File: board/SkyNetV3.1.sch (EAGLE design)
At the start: 48 parts, among them IC2 RF4463PRO, IC3 LPC1769, IC4 BCX17, Q1 32.768KHz, Q2 12MHz, U1 MCP16301T-I/CHY, X2 CONN-SMATHD

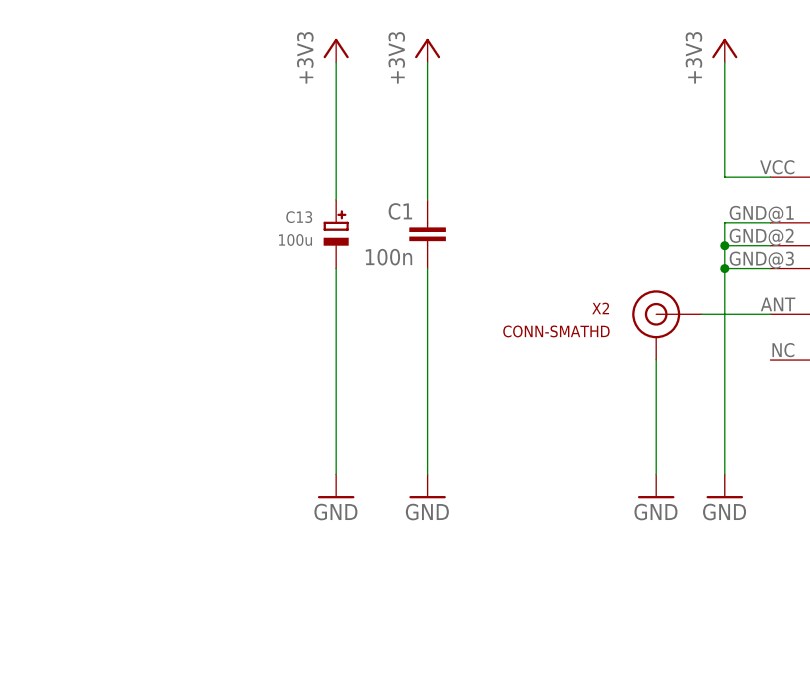
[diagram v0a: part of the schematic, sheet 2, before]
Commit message: improved placement
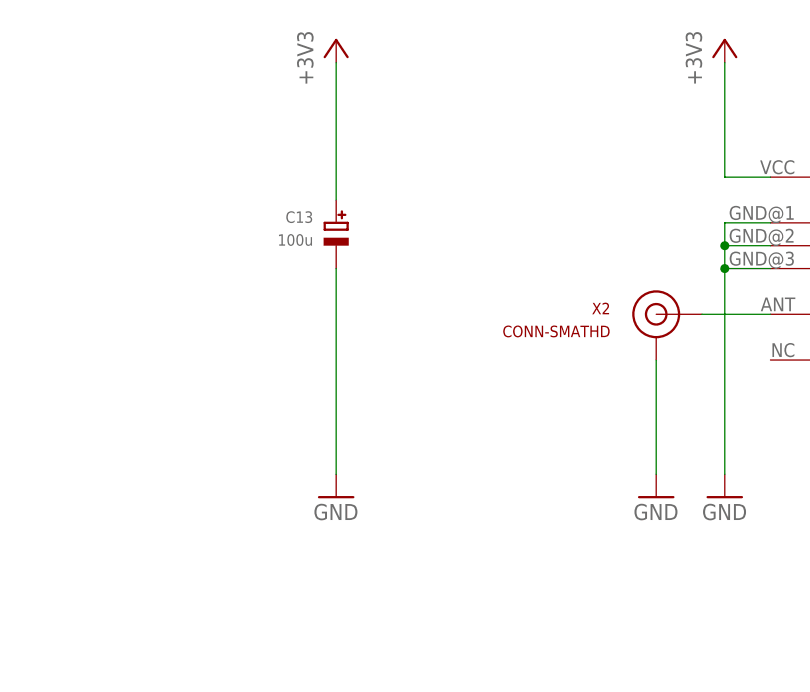
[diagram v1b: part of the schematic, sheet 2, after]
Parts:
- removed C1: 100n, rcl:C-EUC1206K
- C7: value (none) -> 100n
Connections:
- net +3V3: no longer C1.1
- net GND: no longer C1.2
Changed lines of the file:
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@@
 <part name="R5" library="rcl" deviceset="R-EU_" device="R0603" value="10K"/>
 <part name="IC2" library="RF4436PRO" deviceset="RF4463PRO" device=""/>
-<part name="GND10" library="supply1" deviceset="GND" device=""/>
 <part name="+3V1" library="supply1" deviceset="+3V3" device=""/>
 <part name="+3V5" library="supply1" deviceset="+3V3" device=""/>
@@
 <part name="+3V15" library="supply1" deviceset="+3V3" device=""/>
 <part name="R1" library="rcl" deviceset="R-EU_" device="R0603" value="10k"/>
-<part name="C1" library="rcl" deviceset="C-EU" device="C1206K" value="100n"/>
 <part name="P+10" library="supply1" deviceset="+5V" device=""/>
 <part name="GND23" library="supply1" deviceset="GND" device=""/>
@@
 <part name="C6" library="rcl" deviceset="C-EU" device="C0805" value="10u"/>
 <part name="+3V6" library="supply1" deviceset="+3V3" device=""/>
-<part name="+3V7" library="supply1" deviceset="+3V3" device=""/>
 <part name="+3V11" library="supply1" deviceset="+3V3" device=""/>
 <part name="JP3" library="microbuilder" deviceset="HEADER-2X5" device="1.27MM" value="JTAG"/>
@@
 <part name="U1" library="skynet_other" deviceset="MCP16301T-I/CHY" device=""/>
 <part name="GND3" library="supply1" deviceset="GND" device=""/>
-<part name="C7" library="rcl" deviceset="C-EU" device="C0603"/>
+<part name="C7" library="rcl" deviceset="C-EU" device="C0603" value="100n"/>
 <part name="D1" library="microbuilder" deviceset="DIODE" device="SOD-323" value="1N4148 WS"/>
 <part name="B140F" library="diode" deviceset="DIODE-" device="DO214AC"/>
@@
 <instance part="FRAME4" gate="G$1" x="0" y="0"/>
 <instance part="IC2" gate="G$1" x="152.4" y="106.68"/>
-<instance part="GND10" gate="1" x="99.06" y="81.28"/>
-<instance part="C1" gate="G$1" x="99.06" y="111.76" rot="MR0"/>
 <instance part="C13" gate="G$1" x="88.9" y="109.22" rot="MR0"/>
 <instance part="GND19" gate="1" x="88.9" y="81.28"/>
@@
 <instance part="GND32" gate="1" x="124.46" y="81.28"/>
 <instance part="+3V6" gate="G$1" x="88.9" y="132.08"/>
-<instance part="+3V7" gate="G$1" x="99.06" y="132.08"/>
 <instance part="+3V11" gate="G$1" x="132.08" y="132.08"/>
 </instances>
@@
 <nets>
 <net name="GND" class="0">
-<segment>
-<pinref part="C1" gate="G$1" pin="2"/>
-<pinref part="GND10" gate="1" pin="GND"/>
-<wire x1="99.06" y1="83.82" x2="99.06" y2="106.68" width="0.1524" layer="91"/>
-</segment>
 <segment>
 <pinref part="GND19" gate="1" pin="GND"/>
@@
 </segment>
 <segment>
-<pinref part="C1" gate="G$1" pin="1"/>
-<pinref part="+3V7" gate="G$1" pin="+3V3"/>
-<wire x1="99.06" y1="129.54" x2="99.06" y2="114.3" width="0.1524" layer="91"/>
-</segment>
-<segment>

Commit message: almost done
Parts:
- removed C9: 10u, rcl:C-EUC0805
- removed SJ1: RESET, jumper:SJ
- removed USB1: MOLEX-47346-0001, usb_con-update:MOLEX-47346-0001
- added JP1: (no value), jumper:JP1E
- added TP4, TP5: PTR1B1,27, testpad:PTR1B1,27
- added TP6: PTR1B2,54, testpad:PTR1B2,54
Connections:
- net +3V3: now also TP6.TP; no longer C9.1
- net +5V: now also JP1.2; no longer USB1.1
- net GND: now also JP1.1; no longer C9.2, SJ1.1, USB1.5, USB1.GND1, USB1.GND2, USB1.GND3, USB1.GND4
- net RESET: no longer SJ1.2
- net USB-CABLE-D+: now also TP5.TP; no longer USB1.3
- net USB-CABLE-D-: now also TP4.TP; no longer USB1.2
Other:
- moved on the sheet: R2

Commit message: mitten drin
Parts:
- added TP10, TP11, TP12, TP13, TP7, TP8, TP9: PTR1B1,27, testpad:PTR1B1,27
- TP3: value PTR1B1,27 -> PTR1B2,54; device testpad:PTR1B1,27 -> testpad:PTR1B2,54
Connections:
- new net N$10: IC3.P2[13]/EINT3/I2STX_SDA, TP13.TP
- new net N$3: IC3.P2[0]/PWM1[1]/TXD1, TP8.TP
- new net N$5: IC3.P0[9]/I2STX_SDA/MOSI1/MAT2[3], TP9.TP
- new net N$6: IC3.P0[8]/I2STX_WS/MISO1/MAT2[2], TP10.TP
- new net N$7: IC3.P2[1]/PWM1[2]/RXD1, TP7.TP
- new net N$8: IC3.P0[11]/RXD2/SCL2/MAT3[1], TP12.TP
- new net N$9: IC3.P0[10]/TXD2/SDA2/MAT3[0], TP11.TP
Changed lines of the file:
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@@
 <part name="+3V12" library="supply1" deviceset="+3V3" device=""/>
 <part name="GND14" library="supply1" deviceset="GND" device=""/>
-<part name="TP3" library="testpad" deviceset="PTR1" device="B1,27"/>
 <part name="GND1" library="supply1" deviceset="GND" device=""/>
 <part name="U1" library="skynet_other" deviceset="MCP16301T-I/CHY" device=""/>
@@
 <part name="TP6" library="testpad" deviceset="PTR1" device="B2,54"/>
 <part name="+3V7" library="supply1" deviceset="+3V3" device=""/>
+<part name="TP7" library="testpad" deviceset="PTR1" device="B1,27"/>
+<part name="TP8" library="testpad" deviceset="PTR1" device="B1,27"/>
+<part name="TP9" library="testpad" deviceset="PTR1" device="B1,27"/>
+<part name="TP10" library="testpad" deviceset="PTR1" device="B1,27"/>
+<part name="TP11" library="testpad" deviceset="PTR1" device="B1,27"/>
+<part name="TP12" library="testpad" deviceset="PTR1" device="B1,27"/>
+<part name="TP3" library="testpad" deviceset="PTR1" device="B2,54"/>
+<part name="TP13" library="testpad" deviceset="PTR1" device="B1,27"/>
 </parts>
 <sheets>
@@
 <instance part="R1" gate="G$1" x="60.96" y="40.64" rot="R90"/>
 <instance part="SJ2" gate="1" x="215.9" y="45.72" rot="R90"/>
+<instance part="TP7" gate="G$1" x="167.64" y="99.06" rot="R90"/>
+<instance part="TP8" gate="G$1" x="167.64" y="101.6" rot="R90"/>
+<instance part="TP9" gate="G$1" x="45.72" y="142.24" rot="R270"/>
+<instance part="TP10" gate="G$1" x="45.72" y="144.78" rot="R270"/>
+<instance part="TP11" gate="G$1" x="45.72" y="139.7" rot="R270"/>
+<instance part="TP12" gate="G$1" x="45.72" y="137.16" rot="R270"/>
+<instance part="TP13" gate="G$1" x="167.64" y="68.58" rot="R90"/>
 </instances>
 <busses>
@@
 <wire x1="198.12" y1="99.06" x2="223.52" y2="99.06" width="0.1524" layer="91"/>
 <label x="223.52" y="99.06" size="1.27" layer="95" xref="yes"/>
+</segment>
+</net>
+<net name="N$3" class="0">
+<segment>
+<pinref part="IC3" gate="G$1" pin="P2[0]/PWM1[1]/TXD1"/>
+<pinref part="TP8" gate="G$1" pin="TP"/>
+<wire x1="165.1" y1="101.6" x2="160.02" y2="101.6" width="0.1524" layer="91"/>
+</segment>
+</net>
+<net name="N$5" class="0">
+<segment>
+<pinref part="IC3" gate="G$1" pin="P0[9]/I2STX_SDA/MOSI1/MAT2[3]"/>
+<pinref part="TP9" gate="G$1" pin="TP"/>
+<wire x1="48.26" y1="142.24" x2="71.12" y2="142.24" width="0.1524" layer="91"/>
+</segment>
+</net>
+<net name="N$6" class="0">
+<segment>
+<pinref part="IC3" gate="G$1" pin="P0[8]/I2STX_WS/MISO1/MAT2[2]"/>
+<pinref part="TP10" gate="G$1" pin="TP"/>
+<wire x1="48.26" y1="144.78" x2="71.12" y2="144.78" width="0.1524" layer="91"/>
+</segment>
+</net>
+<net name="N$7" class="0">
+<segment>
+<pinref part="IC3" gate="G$1" pin="P2[1]/PWM1[2]/RXD1"/>
+<pinref part="TP7" gate="G$1" pin="TP"/>
+<wire x1="165.1" y1="99.06" x2="160.02" y2="99.06" width="0.1524" layer="91"/>
+</segment>
+</net>
+<net name="N$8" class="0">
+<segment>
+<pinref part="IC3" gate="G$1" pin="P0[11]/RXD2/SCL2/MAT3[1]"/>
+<pinref part="TP12" gate="G$1" pin="TP"/>
+<wire x1="48.26" y1="137.16" x2="71.12" y2="137.16" width="0.1524" layer="91"/>
+</segment>
+</net>
+<net name="N$9" class="0">
+<segment>
+<pinref part="IC3" gate="G$1" pin="P0[10]/TXD2/SDA2/MAT3[0]"/>
+<pinref part="TP11" gate="G$1" pin="TP"/>
+<wire x1="48.26" y1="139.7" x2="71.12" y2="139.7" width="0.1524" layer="91"/>
+</segment>
+</net>
+<net name="N$10" class="0">
+<segment>
+<pinref part="IC3" gate="G$1" pin="P2[13]/EINT3/I2STX_SDA"/>
+<pinref part="TP13" gate="G$1" pin="TP"/>
+<wire x1="165.1" y1="68.58" x2="160.02" y2="68.58" width="0.1524" layer="91"/>
 </segment>
 </net>
@@
 <instance part="+3V12" gate="G$1" x="45.72" y="71.12"/>
 <instance part="GND14" gate="1" x="45.72" y="33.02"/>
-<instance part="TP3" gate="G$1" x="195.58" y="48.26" rot="R270"/>
 <instance part="GND1" gate="1" x="203.2" y="40.64"/>
 <instance part="TP4" gate="G$1" x="35.56" y="139.7" rot="R270"/>
@@
 <instance part="TP6" gate="G$1" x="200.66" y="106.68" rot="R90"/>
 <instance part="+3V7" gate="G$1" x="195.58" y="106.68" rot="MR270"/>
+<instance part="TP3" gate="G$1" x="195.58" y="48.26" rot="R270"/>
 </instances>
 <busses>
@@
 </segment>
 <segment>
-<pinref part="TP3" gate="G$1" pin="TP"/>
 <pinref part="GND1" gate="1" pin="GND"/>
 <wire x1="198.12" y1="48.26" x2="203.2" y2="48.26" width="0.1524" layer="91"/>
 <wire x1="203.2" y1="48.26" x2="203.2" y2="43.18" width="0.1524" layer="91"/>
-</segment>
-</net>
+<pinref part="TP3" gate="G$1" pin="TP"/>
+</segment>
+</net>

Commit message: done
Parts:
- removed C18: 100n, rcl:C-EUC0603
- removed LED2: RGBLED5050, adafruit:RGBLED5050
- removed R18, R19: 68, rcl:R-EU_R0603
- added LED1: (no value), led:LEDCHIP-LED0805
- R17: value 100 -> 360
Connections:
- removed net LED-B: IC3.P1[18]/USB_UP_LED/PWM1[1]/CAP1[0], LED2.BLUE_C
- removed net LED-B-R: LED2.BLUE_A, R19.1
- removed net LED-G: IC3.P1[21]/MCABORT/PWM1[3]/SSEL0, LED2.GREEN_C
- removed net LED-G-R: LED2.GREEN_A, R18.1
- removed net LED-R: IC3.P1[20]/MCI0/PWM1[2]/SCK0, LED2.RED_C
- new net LED: IC3.P1[21]/MCABORT/PWM1[3]/SSEL0, LED1.C
- net +3V3: no longer C18.1, R18.2, R19.2
- net GND: no longer C18.2
- net LED-R-R: now also LED1.A; no longer LED2.RED_A
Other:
- note removed: "TODO: I2C ADC??"
- moved on the sheet: TP6
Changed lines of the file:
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@@
 <part name="IC3" library="lpc1xxx-v6" deviceset="LPC1768" device="" value="LPC1769"/>
 <part name="FRAME1" library="frames" deviceset="A4L-LOC" device="" value="SkyNet Main"/>
-<part name="C18" library="rcl" deviceset="C-EU" device="C0603" value="100n"/>
-<part name="GND4" library="supply1" deviceset="GND" device=""/>
 <part name="Q2" library="skynet_other" deviceset="XTAL" device="4-PAD" value="12MHz"/>
 <part name="Q1" library="skynet_other" deviceset="XTAL" device="2-PAD" value="32.768KHz"/>
@@
 <part name="R5" library="rcl" deviceset="R-EU_" device="R0603" value="10K"/>
 <part name="IC2" library="RF4436PRO" deviceset="RF4463PRO" device=""/>
-<part name="+3V1" library="supply1" deviceset="+3V3" device=""/>
 <part name="+3V5" library="supply1" deviceset="+3V3" device=""/>
 <part name="IC4" library="skynet_other" deviceset="BCX17" device=""/>
@@
 <part name="R4" library="rcl" deviceset="R-EU_" device="R0603" value="1k5"/>
 <part name="GND26" library="supply1" deviceset="GND" device=""/>
-<part name="R19" library="rcl" deviceset="R-EU_" device="R0603" value="68"/>
-<part name="R17" library="rcl" deviceset="R-EU_" device="R0603" value="100"/>
-<part name="R18" library="rcl" deviceset="R-EU_" device="R0603" value="68"/>
+<part name="R17" library="rcl" deviceset="R-EU_" device="R0603" value="360"/>
 <part name="R2" library="rcl" deviceset="R-EU_" device="R0603" value="10K"/>
 <part name="+3V2" library="supply1" deviceset="+3V3" device=""/>
@@
 <part name="GND17" library="supply1" deviceset="GND" device=""/>
 <part name="+3V18" library="supply1" deviceset="+3V3" device=""/>
-<part name="LED2" library="adafruit" deviceset="RGBLED" device="5050"/>
 <part name="SJ2" library="jumper" deviceset="SJ" device="" value="PROG"/>
 <part name="C13" library="microbuilder" deviceset="CAP_TANTALUM" device="C/6032_WAVE" value="100u"/>
@@
 <part name="TP3" library="testpad" deviceset="PTR1" device="B2,54"/>
 <part name="TP13" library="testpad" deviceset="PTR1" device="B1,27"/>
+<part name="LED1" library="led" deviceset="LED" device="CHIP-LED0805"/>
 </parts>
 <sheets>
@@
 </segment>
 </net>
-<net name="LED-R" class="0">
-<segment>
-<pinref part="IC3" gate="G$1" pin="P1[20]/MCI0/PWM1[2]/SCK0"/>
-<wire x1="160.02" y1="134.62" x2="226.06" y2="134.62" width="0.1524" layer="91"/>
-<label x="226.06" y="134.62" size="1.778" layer="95" xref="yes"/>
-</segment>
-</net>
 <net name="PROG" class="0">
 <segment>
@@
 </segment>
 </net>
-<net name="LED-B" class="0">
-<segment>
-<pinref part="IC3" gate="G$1" pin="P1[18]/USB_UP_LED/PWM1[1]/CAP1[0]"/>
-<wire x1="160.02" y1="139.7" x2="226.06" y2="139.7" width="0.1524" layer="91"/>
-<label x="226.06" y="139.7" size="1.778" layer="95" xref="yes"/>
-</segment>
-</net>
-<net name="LED-G" class="0">
+<net name="LED" class="0">
 <segment>
 <pinref part="IC3" gate="G$1" pin="P1[21]/MCABORT/PWM1[3]/SSEL0"/>
@@
 <instance part="GND23" gate="1" x="76.2" y="60.96"/>
 <instance part="FRAME3" gate="G$1" x="0" y="0"/>
-<instance part="C18" gate="G$1" x="228.6" y="73.66"/>
-<instance part="GND4" gate="1" x="228.6" y="63.5"/>
-<instance part="+3V1" gate="G$1" x="228.6" y="81.28"/>
 <instance part="C19" gate="G$1" x="228.6" y="45.72"/>
 <instance part="GND2" gate="1" x="228.6" y="35.56"/>
@@
 </segment>
 <segment>
-<pinref part="GND4" gate="1" pin="GND"/>
-<pinref part="C18" gate="G$1" pin="2"/>
-<wire x1="228.6" y1="66.04" x2="228.6" y2="68.58" width="0.1524" layer="91"/>
-</segment>
-<segment>
 <pinref part="GND2" gate="1" pin="GND"/>
 <pinref part="C19" gate="G$1" pin="2"/>
@@
 </net>
 <net name="+3V3" class="0">
-<segment>
-<pinref part="C18" gate="G$1" pin="1"/>
-<pinref part="+3V1" gate="G$1" pin="+3V3"/>
-<wire x1="228.6" y1="76.2" x2="228.6" y2="78.74" width="0.1524" layer="91"/>
-</segment>
 <segment>
 <pinref part="C19" gate="G$1" pin="1"/>
@@
 <text x="134.62" y="7.62" size="1.778" layer="94">Prog alternative</text>
 <text x="7.62" y="7.62" size="1.778" layer="94">JTAG</text>
-<text x="7.62" y="170.18" size="1.778" layer="91">TODO: I2C ADC??</text>
 </plain>
 <instances>
@@
 <instance part="C23" gate="G$1" x="78.74" y="129.54"/>
 <instance part="FRAME2" gate="G$1" x="0" y="0"/>
-<instance part="R19" gate="G$1" x="213.36" y="121.92"/>
 <instance part="R17" gate="G$1" x="213.36" y="142.24"/>
-<instance part="R18" gate="G$1" x="213.36" y="132.08"/>
 <instance part="+3V14" gate="G$1" x="220.98" y="152.4" rot="MR0"/>
-<instance part="LED2" gate="G$1" x="198.12" y="132.08" rot="R180"/>
 <instance part="GND39" gate="1" x="40.64" y="114.3"/>
 <instance part="GND40" gate="1" x="68.58" y="114.3"/>
@@
 <instance part="TP5" gate="G$1" x="35.56" y="137.16" rot="R270"/>
 <instance part="JP1" gate="A" x="33.02" y="129.54" rot="R90"/>
-<instance part="TP6" gate="G$1" x="200.66" y="106.68" rot="R90"/>
-<instance part="+3V7" gate="G$1" x="195.58" y="106.68" rot="MR270"/>
+<instance part="TP6" gate="G$1" x="195.58" y="63.5" rot="R270"/>
+<instance part="+3V7" gate="G$1" x="203.2" y="76.2" rot="MR0"/>
 <instance part="TP3" gate="G$1" x="195.58" y="48.26" rot="R270"/>
+<instance part="LED1" gate="G$1" x="203.2" y="142.24" rot="R270"/>
 </instances>
 <busses>
@@
 <net name="+3V3" class="0">
 <segment>
-<pinref part="R19" gate="G$1" pin="2"/>
-<wire x1="218.44" y1="121.92" x2="220.98" y2="121.92" width="0.1524" layer="91"/>
-<wire x1="220.98" y1="121.92" x2="220.98" y2="132.08" width="0.1524" layer="91"/>
 <pinref part="R17" gate="G$1" pin="2"/>
-<wire x1="220.98" y1="132.08" x2="220.98" y2="142.24" width="0.1524" layer="91"/>
 <wire x1="220.98" y1="142.24" x2="218.44" y2="142.24" width="0.1524" layer="91"/>
-<pinref part="R18" gate="G$1" pin="2"/>
-<wire x1="218.44" y1="132.08" x2="220.98" y2="132.08" width="0.1524" layer="91"/>
-<junction x="220.98" y="132.08"/>
 <pinref part="+3V14" gate="G$1" pin="+3V3"/>
 <wire x1="220.98" y1="142.24" x2="220.98" y2="149.86" width="0.1524" layer="91"/>
-<junction x="220.98" y="142.24"/>
 </segment>
 <segment>
@@
 <pinref part="TP6" gate="G$1" pin="TP"/>
 <pinref part="+3V7" gate="G$1" pin="+3V3"/>
+<wire x1="198.12" y1="63.5" x2="203.2" y2="63.5" width="0.1524" layer="91"/>
+<wire x1="203.2" y1="63.5" x2="203.2" y2="73.66" width="0.1524" layer="91"/>
 </segment>
 </net>
@@
 <segment>
 <pinref part="R17" gate="G$1" pin="1"/>
-<wire x1="203.2" y1="137.16" x2="205.74" y2="137.16" width="0.1524" layer="91"/>
-<wire x1="205.74" y1="137.16" x2="205.74" y2="142.24" width="0.1524" layer="91"/>
 <wire x1="205.74" y1="142.24" x2="208.28" y2="142.24" width="0.1524" layer="91"/>
-<pinref part="LED2" gate="G$1" pin="RED_A"/>
-</segment>
-</net>
-<net name="LED-G-R" class="0">
-<segment>
-<pinref part="R18" gate="G$1" pin="1"/>
-<wire x1="208.28" y1="132.08" x2="203.2" y2="132.08" width="0.1524" layer="91"/>
-<pinref part="LED2" gate="G$1" pin="GREEN_A"/>
-</segment>
-</net>
-<net name="LED-B-R" class="0">
-<segment>
-<pinref part="R19" gate="G$1" pin="1"/>
-<wire x1="203.2" y1="127" x2="205.74" y2="127" width="0.1524" layer="91"/>
-<wire x1="205.74" y1="127" x2="205.74" y2="121.92" width="0.1524" layer="91"/>
-<wire x1="205.74" y1="121.92" x2="208.28" y2="121.92" width="0.1524" layer="91"/>
-<pinref part="LED2" gate="G$1" pin="BLUE_A"/>
-</segment>
-</net>
-<net name="LED-R" class="0">
-<segment>
-<wire x1="193.04" y1="137.16" x2="187.96" y2="137.16" width="0.1524" layer="91"/>
-<label x="187.96" y="137.16" size="1.778" layer="95" rot="R180" xref="yes"/>
-<pinref part="LED2" gate="G$1" pin="RED_C"/>
-</segment>
-</net>
-<net name="LED-G" class="0">
-<segment>
-<label x="187.96" y="132.08" size="1.778" layer="95" rot="R180" xref="yes"/>
-<pinref part="LED2" gate="G$1" pin="GREEN_C"/>
-<wire x1="193.04" y1="132.08" x2="187.96" y2="132.08" width="0.1524" layer="91"/>
-</segment>
-</net>
-<net name="LED-B" class="0">
-<segment>
-<wire x1="193.04" y1="127" x2="187.96" y2="127" width="0.1524" layer="91"/>
-<label x="187.96" y="127" size="1.778" layer="95" rot="R180" xref="yes"/>
-<pinref part="LED2" gate="G$1" pin="BLUE_C"/>
+<pinref part="LED1" gate="G$1" pin="A"/>
 </segment>
 </net>
@@
 </segment>
 </net>
+<net name="LED" class="0">
+<segment>
+<pinref part="LED1" gate="G$1" pin="C"/>
+<wire x1="198.12" y1="142.24" x2="190.5" y2="142.24" width="0.1524" layer="91"/>
+<label x="190.5" y="142.24" size="1.778" layer="95" rot="R180" xref="yes"/>
+</segment>
+</net>
